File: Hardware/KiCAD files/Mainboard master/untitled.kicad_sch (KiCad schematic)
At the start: 23 parts, among them J1 Conn_01x02, J32 JST_03, J33 Conn_01x04, Q2 2DD1664, SW8 Push_Button, SW9 Push_Button, U11 PCA9534PW, U12 ESP32-S3-WROOM-1, U3 PCA9534PW

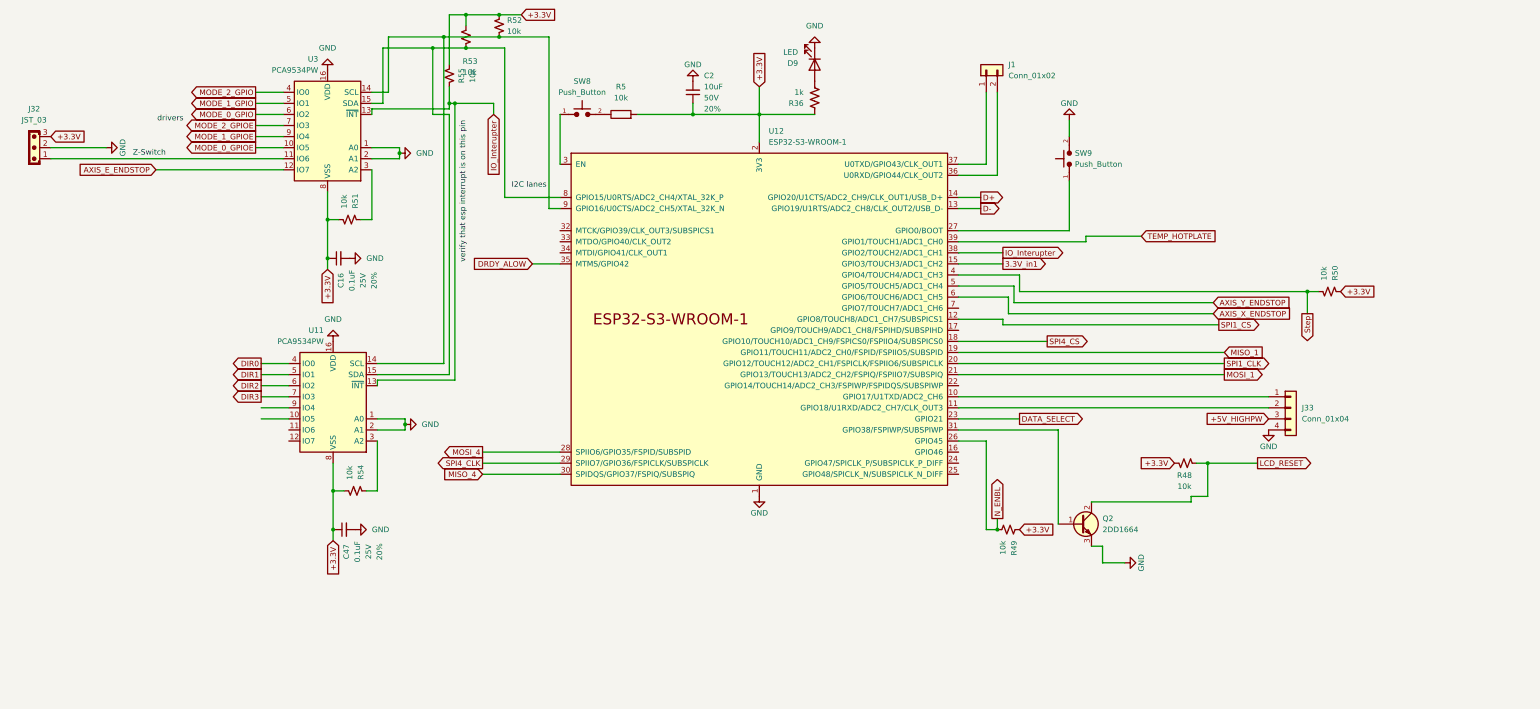
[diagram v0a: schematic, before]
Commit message: general updates to the schematics and layouts
includes some backchecks tot he master schematic to be accurate for the paper
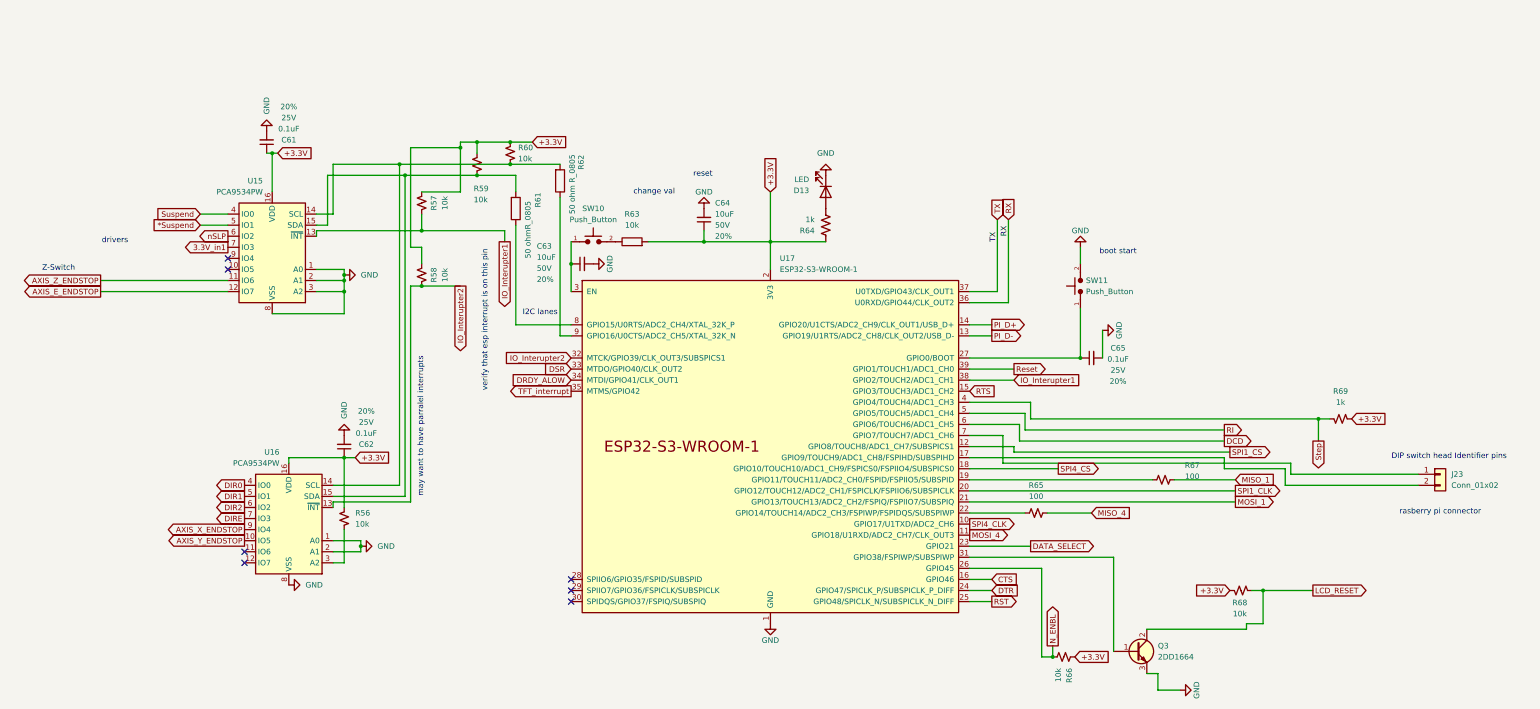
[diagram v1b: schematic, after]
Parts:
- removed C16, C47: 0.1uF, PCM_SparkFun-Capacitor:C_0603_1608Metric, symbol PCM_SparkFun-Capacitor:0.1uF_0603_25V_20%
- removed C2: 10uF, PCM_SparkFun-Capacitor:C_1210_3225Metric, symbol PCM_SparkFun-Capacitor:10uF_1210_50V_20%
- removed D9: LED, LED_SMD:LED_0603_1608Metric, symbol Device:LED
- removed J1: Conn_01x02, PCM_SparkFun-Connector:1x02_P2.54mm, symbol PCM_SparkFun-Connector:Conn_01x02_P2.54mm
- removed J32: JST_03, Connector_JST:JST_EH_B3B-EH-A_1x03_P2.50mm_Vertical, symbol PCM_SL_Connectors:JST_03
- removed J33: Conn_01x04, PCM_SparkFun-Connector:1x04_P2.54mm, symbol PCM_SparkFun-Connector:Conn_01x04_P2.54mm
- removed Q2: 2DD1664, PCM_Package_TO_SOT_SMD_AKL:SOT-89-3, symbol PCM_Transistor_BJT_AKL:2DD1664
- removed R36: 1k, Resistor_SMD:R_1206_3216Metric_Pad1.30x1.75mm_HandSolder, symbol Device:R_US
- removed R48, R49, R50, R51, R52, R53, R54, R55: 10k, PCM_SparkFun-Resistor:R_0603_1608Metric, symbol PCM_SparkFun-Resistor:10k_0603
- removed R5: 10k, Resistor_THT:R_Axial_DIN0207_L6.3mm_D2.5mm_P10.16mm_Horizontal, symbol PCM_SL_Resistors:10k
- removed SW8, SW9: Push_Button, Button_Switch_THT:SW_PUSH_6mm, symbol PCM_SL_Devices:Push_Button
- removed U11, U3: PCA9534PW, PCM_SparkFun-Semiconductor-Standard:TSSOP-16_4.4x5mm_P0.65mm, symbol PCM_SparkFun-IC-Special-Function:PCA9534PW
- removed U12: ESP32-S3-WROOM-1, PCM_Espressif:ESP32-S3-WROOM-1, symbol PCM_Espressif:ESP32-S3-WROOM-1
- added C61, C62, C65: 0.1uF, PCM_SparkFun-Capacitor:C_0603_1608Metric, symbol PCM_SparkFun-Capacitor:0.1uF_0603_25V_20%
- added C63, C64: 10uF, PCM_SparkFun-Capacitor:C_1210_3225Metric, symbol PCM_SparkFun-Capacitor:10uF_1210_50V_20%
- added D13: LED, LED_SMD:LED_0603_1608Metric, symbol Device:LED
- added J23: Conn_01x02, PCM_SparkFun-Connector:1x02_P2.54mm, symbol PCM_SparkFun-Connector:Conn_01x02_P2.54mm
- added Q3: 2DD1664, PCM_Package_TO_SOT_SMD_AKL:SOT-89-3, symbol PCM_Transistor_BJT_AKL:2DD1664
- added R56, R57, R58, R59, R60, R66, R68: 10k, PCM_SparkFun-Resistor:R_0603_1608Metric, symbol PCM_SparkFun-Resistor:10k_0603
- added R61: 50 ohmR_0805, PCM_Resistor_SMD_AKL:R_0805_2012Metric, symbol PCM_Resistor_AKL:R_0805
- added R62: 50 ohm R_0805, PCM_Resistor_SMD_AKL:R_0805_2012Metric, symbol PCM_Resistor_AKL:R_0805
- added R63: 10k, Resistor_THT:R_Axial_DIN0207_L6.3mm_D2.5mm_P10.16mm_Horizontal, symbol PCM_SL_Resistors:10k
- added R64: 1k, Resistor_SMD:R_1206_3216Metric_Pad1.30x1.75mm_HandSolder, symbol Device:R_US
- added R65, R67: 100, PCM_SparkFun-Resistor:R_0603_1608Metric, symbol PCM_SparkFun-Resistor:100_0603
- added R69: 1k, PCM_SparkFun-Resistor:R_0603_1608Metric, symbol PCM_SparkFun-Resistor:10k_0603
- added SW10, SW11: Push_Button, Button_Switch_THT:SW_PUSH_6mm, symbol PCM_SL_Devices:Push_Button
- added U15, U16: PCA9534PW, PCM_SparkFun-Semiconductor-Standard:TSSOP-16_4.4x5mm_P0.65mm, symbol PCM_SparkFun-IC-Special-Function:PCA9534PW
- added U17: ESP32-S3-WROOM-1, PCM_Espressif:ESP32-S3-WROOM-1, symbol PCM_Espressif:ESP32-S3-WROOM-1
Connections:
- net +3.3V: now also C61.1, C62.1, C64.1, R56.2, R57.1, R58.1, R59.2, R60.2, R63.1, R64.1, R66.2, R68.1, R69.2, U15.16 (VDD), U16.16 (VDD), U17.2 (3V3)
- net 3.3V_in1: now also U15.7 (IO3)
- net AXIS_E_ENDSTOP: now also U15.12 (IO7)
- net AXIS_X_ENDSTOP: now also U16.9 (IO4)
- net AXIS_Y_ENDSTOP: now also U16.10 (IO5)
- net DATA_SELECT: now also U17.23 (GPIO21)
- net DIR0: now also U16.4 (IO0)
- net DIR1: now also U16.5 (IO1)
- net DIR2: now also U16.6 (IO2)
- net DRDY_ALOW: now also U17.34 (MTDI/GPIO41/CLK_OUT1)
- net GND: now also C61.2, C62.2, C63.2, C64.2, C65.2, D13.1 (K), Q3.3 (E), SW11.2, U15.1 (A0), U15.2 (A1), U15.3 (A2), U15.8 (VSS), U16.1 (A0), U16.2 (A1), U16.8 (VSS), U17.1 (GND), U17.40 (GND), U17.41 (GND)
- net LCD_RESET: now also Q3.2 (C), R68.2
- net MISO_1: now also R67.2
- net MISO_4: now also R65.2
- net MOSI_1: now also U17.21 (GPIO13/TOUCH13/ADC2_CH2/FSPIQ/FSPIIO7/SUBSPIQ)
- net MOSI_4: now also U17.11 (GPIO18/U1RXD/ADC2_CH7/CLK_OUT3)
- net N_ENBL: now also R66.1, U17.26 (GPIO45)
- net SPI1_CLK: now also U17.20 (GPIO12/TOUCH12/ADC2_CH1/FSPICLK/FSPIIO6/SUBSPICLK)
- net SPI1_CS: now also U17.12 (GPIO8/TOUCH8/ADC1_CH7/SUBSPICS1)
- net SPI4_CLK: now also U17.10 (GPIO17/U1TXD/ADC2_CH6)
- net SPI4_CS: now also U17.18 (GPIO10/TOUCH10/ADC1_CH9/FSPICS0/FSPIIO4/SUBSPICS0)
- net Step: now also R69.1, U17.4 (GPIO4/TOUCH4/ADC1_CH3)
- new net: C65.1, SW11.1, U17.27 (GPIO0/BOOT)
- new net: R59.1, R61.1, U15.15 (SDA), U16.15 (SDA)
- new net: R61.2, U17.8 (GPIO15/U0RTS/ADC2_CH4/XTAL_32K_P)
- new net: R63.2, SW10.2
- new net: D13.2 (A), R64.2
- new net: Q3.1 (B), U17.31 (GPIO38/FSPIWP/SUBSPIWP)
- new net: J23.2 (Pin_2), U17.17 (GPIO9/TOUCH9/ADC1_CH8/FSPIHD/SUBSPIHD)
- new net: R67.1, U17.19 (GPIO11/TOUCH11/ADC2_CH0/FSPID/FSPIIO5/SUBSPID)
- new net: R65.1, U17.22 (GPIO14/TOUCH14/ADC2_CH3/FSPIWP/FSPIDQS/SUBSPIWP)
- new net: C63.1, SW10.1, U17.3 (EN)
- new net: J23.1 (Pin_1), U17.7 (GPIO7/TOUCH7/ADC1_CH6)
- new net: R62.2, U17.9 (GPIO16/U0CTS/ADC2_CH5/XTAL_32K_N)
- new net: R60.1, R62.1, U15.14 (SCL), U16.14 (SCL)
- new net: R56.1, U16.3 (A2)
- new net *Suspend: U15.5 (IO1)
- new net AXIS_Z_ENDSTOP: U15.11 (IO6)
- new net CTS: U17.16 (GPIO46)
- new net DCD: U17.6 (GPIO6/TOUCH6/ADC1_CH5)
- new net DIRE: U16.7 (IO3)
- new net DSR: U17.33 (MTDO/GPIO40/CLK_OUT2)
- new net DTR: U17.24 (GPIO47/SPICLK_P/SUBSPICLK_P_DIFF)
- new net IO_Interupter1: R57.2, U15.13 (~{INT}), U17.38 (GPIO2/TOUCH2/ADC1_CH1)
- new net IO_Interupter2: R58.2, U16.13 (~{INT}), U17.32 (MTCK/GPIO39/CLK_OUT3/SUBSPICS1)
- new net PI_D+: U17.14 (GPIO20/U1CTS/ADC2_CH9/CLK_OUT1/USB_D+)
- new net PI_D-: U17.13 (GPIO19/U1RTS/ADC2_CH8/CLK_OUT2/USB_D-)
- new net RI: U17.5 (GPIO5/TOUCH5/ADC1_CH4)
- new net RST: U17.25 (GPIO48/SPICLK_N/SUBSPICLK_N_DIFF)
- new net RTS: U17.15 (GPIO3/TOUCH3/ADC1_CH2)
- new net RX: U17.36 (U0RXD/GPIO44/CLK_OUT2)
- new net Reset: U17.39 (GPIO1/TOUCH1/ADC1_CH0)
- new net Suspend: U15.4 (IO0)
- new net TFT_interrupt: U17.35 (MTMS/GPIO42)
- new net TX: U17.37 (U0TXD/GPIO43/CLK_OUT1)
- new net nSLP: U15.6 (IO2)
- no-connect marks 0 -> 7
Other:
- note added: "DIP switch head Identifier pins"
- note added: "boot start"
- note added: "change val"
- note added: "may want to have parralel interrupts"
- note added: "rasberry pi connector"
- note added: "reset"
